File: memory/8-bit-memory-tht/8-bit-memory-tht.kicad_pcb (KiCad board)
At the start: 2 copper layers, 126 parts, among them J1 J1-1_bit_bus, J2 J8-8_bit_bus_connector, J3 J2-2_pole_connector, J4 J8-8_bit_bus_connector, Q1 2N7000, Q10 2N7000, Q11 2N7000, Q12 2N7000, Q13 2N7000, Q14 2N7000, Q15 2N7000, Q16 2N7000, Q17 2N7000, Q18 2N7000, Q19 2N7000, Q2 2N7000, Q20 2N7000, Q21 2N7000, Q22 2N7000, Q23 2N7000, Q24 2N7000, Q25 2N7000, Q26 2N7000, Q27 2N7000, Q28 2N7000, Q29 2N7000, Q3 2N7000, Q30 2N7000, Q31 2N7000, Q32 2N7000, Q33 2N7000, Q34 2N7000, Q35 2N7000, Q36 2N7000, Q37 2N7000, Q38 2N7000, Q39 2N7000, Q4 2N7000, Q40 2N7000, Q41 2N7000, Q42 2N7000, Q43 2N7000, Q44 2N7000, Q45 2N7000, Q46 2N7000, Q47 2N7000, Q48 2N7000, Q49 2N7000, Q5 2N7000, Q50 2N7000, Q51 2N7000, Q52 2N7000, Q53 2N7000, Q54 2N7000, Q55 2N7000, Q56 2N7000, Q57 2N7000, Q58 2N7000, Q59 2N7000, Q6 2N7000, Q60 2N7000, Q61 2N7000, Q62 2N7000, Q63 2N7000, Q64 2N7000, Q65 2N7000, Q66 2N7000, Q67 2N7000, Q68 2N7000, Q69 2N7000, Q7 2N7000, Q70 2N7000, Q71 2N7000, Q72 2N7000, Q73 2N7000, Q8 2N7000, Q9 2N7000

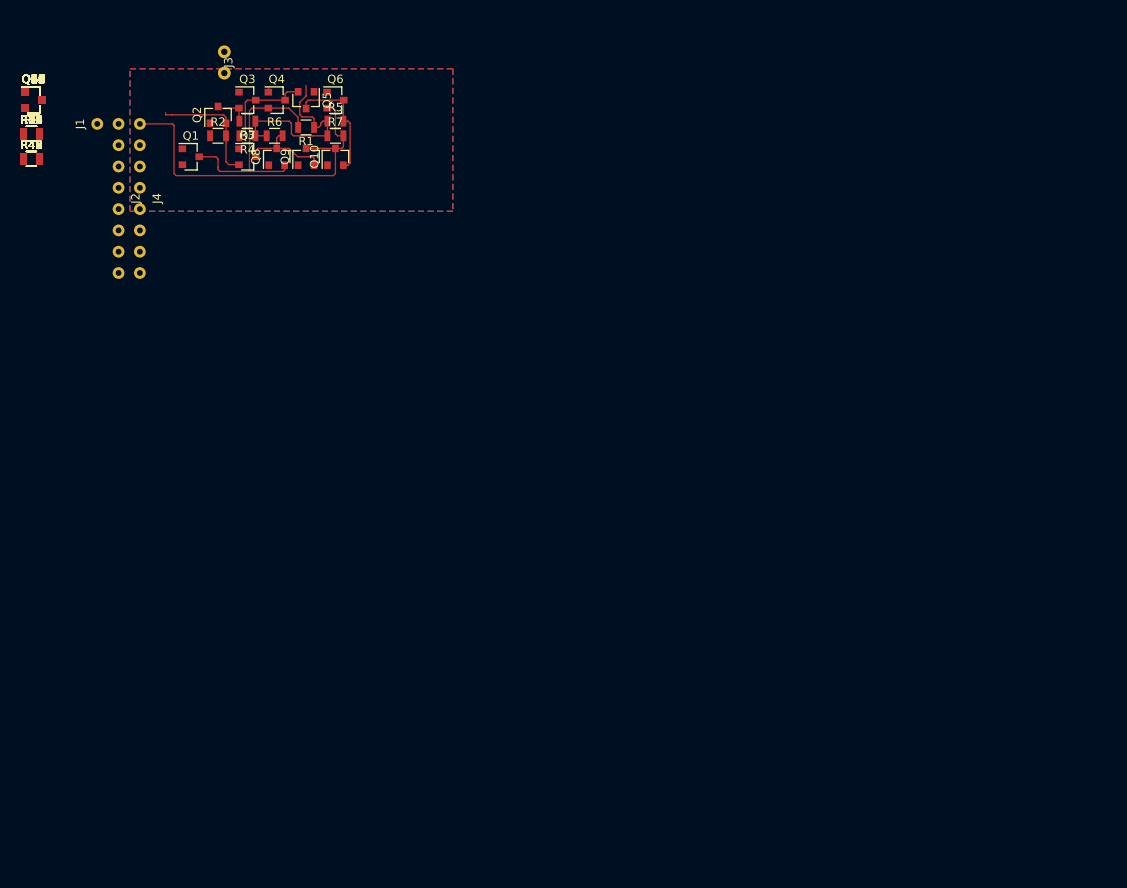
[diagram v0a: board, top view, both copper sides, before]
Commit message: Finish THT memory board layout
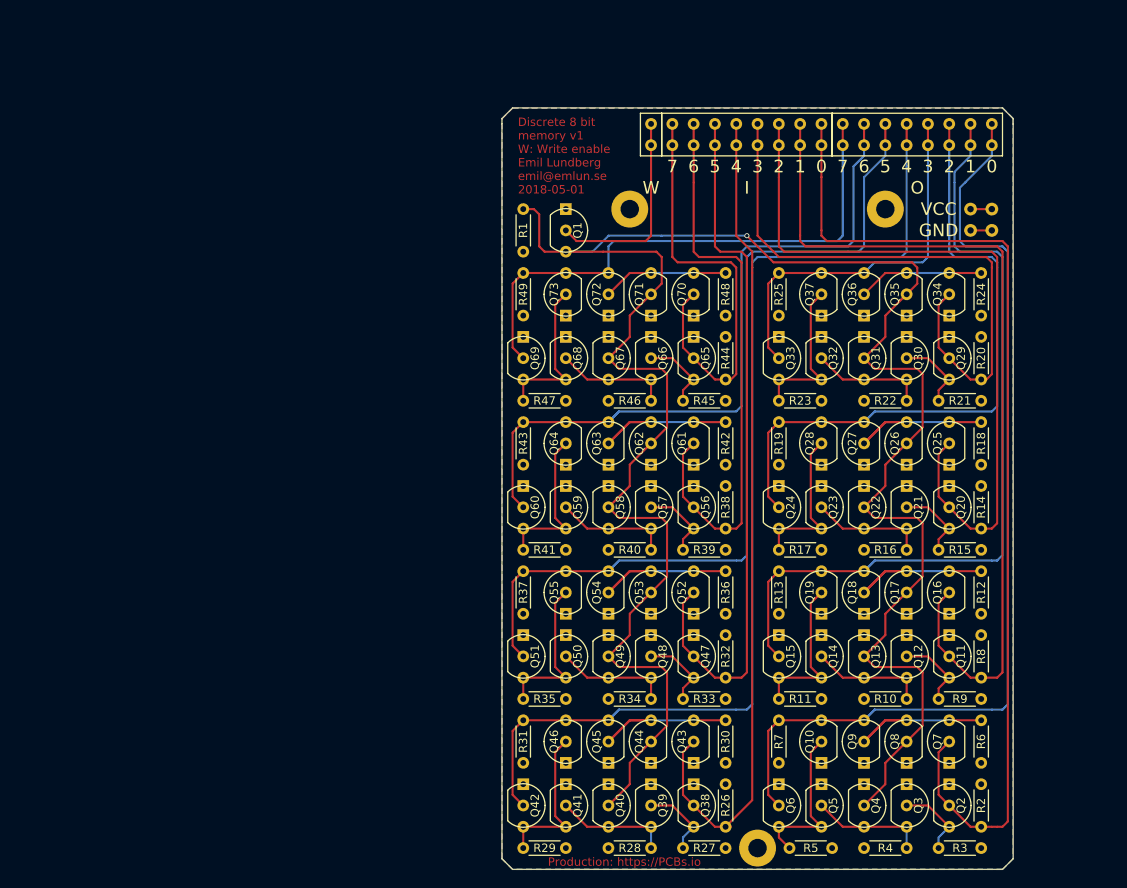
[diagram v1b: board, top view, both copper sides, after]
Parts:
- added REF**: MountingHole_2.2mm_M2_Pad, Mounting_Holes:MountingHole_2.2mm_M2_Pad, F.Cu at (165.1, 78.7)
- added REF**: MountingHole_2.2mm_M2_Pad, Mounting_Holes:MountingHole_2.2mm_M2_Pad, F.Cu at (195.6, 78.7)
- added REF**: MountingHole_2.2mm_M2_Pad, Mounting_Holes:MountingHole_2.2mm_M2_Pad, F.Cu at (180.3, 154.9)
- J1: footprint emlun:J1-1_bit_bus -> J1x2-double_1_bit_bus
- J2, J4: footprint emlun:J8-8_bit_bus_connector -> emlun:J8x2-double_8_bit_bus_connector
- J3: footprint emlun:J2-2_pole_connector -> J2x2-double_2_pole_connector
- Q1, Q10, Q11, Q12, Q13, Q14, Q15, Q16, Q17, Q18, Q19, Q2, Q20, Q21, Q22, Q23, Q24, Q25, Q26, Q27, Q28, Q29, Q3, Q30, Q31, Q32, Q33, Q35, Q36, Q37, Q38, Q39, Q4, Q40, Q41, Q42, Q43, Q44, Q45, Q46, Q47, Q48, Q49, Q5, Q50, Q51, Q52, Q53, Q54, Q55, Q56, Q57, Q58, Q59, Q6, Q60, Q61, Q62, Q63, Q64, Q65, Q66, Q67, Q68, Q69, Q7, Q70, Q71, Q72, Q73, Q8, Q9: footprint TO_SOT_Packages_SMD:SOT-23 -> electrokit:TO-92_Molded_Wide_Inline
- Q34: footprint TO_SOT_Packages_SMD:SOT-23 -> TO-92_Molded_Wide_Inline
- R1, R10, R11, R12, R13, R14, R15, R16, R17, R18, R19, R2, R20, R21, R22, R23, R24, R25, R26, R27, R28, R29, R3, R30, R31, R32, R33, R34, R35, R36, R37, R38, R39, R4, R40, R41, R42, R43, R44, R45, R46, R47, R48, R49, R5, R6, R7, R8, R9: footprint Resistors_SMD:R_0805 -> emlun:R_Axial_DIN0204_L3.6mm_D1.6mm_P5.08mm_Horizontal
- moved R9 131.8 mm to (207.0, 137.2), turned to 180 degrees
- moved R8 128.1 mm to (207.0, 129.5), turned to 270 degrees
- moved Q11 127.8 mm to (203.2, 132.1), turned to 270 degrees
- moved R12 126.9 mm to (207.0, 127.0), turned to 90 degrees
- moved Q16 124.0 mm to (203.2, 124.5), turned to 90 degrees
- moved R15 123.7 mm to (207.0, 119.4), turned to 180 degrees
- moved Q12 123.5 mm to (198.1, 132.1), turned to 270 degrees
- moved R3 123.2 mm to (207.0, 154.9)
- moved R14 120.8 mm to (207.0, 111.8), turned to 270 degrees
- moved R10 120.0 mm to (193.0, 137.2)
- moved Q2 119.9 mm to (203.2, 149.9), turned to 270 degrees
- moved R18 119.9 mm to (207.0, 109.2), turned to 90 degrees
- moved Q17 119.5 mm to (198.1, 124.5), turned to 90 degrees
- moved Q20 119.5 mm to (203.2, 114.3), turned to 270 degrees
- moved R2 119.4 mm to (207.0, 147.3), turned to 270 degrees
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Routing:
- net /notW: track 27.2 -> 252.8 mm, vias 0 -> 1
- net /O4: track 0.00 -> 128.0 mm
- net /I0: track 14.6 -> 122.3 mm
- net /O5: track 0.00 -> 106.2 mm
- net /I1: track 0.00 -> 105.8 mm
- net /I4: track 0.00 -> 100.1 mm
- net /O1: track 0.00 -> 97.7 mm
- net /I2: track 0.00 -> 89.3 mm
- net /O6: track 0.00 -> 86.6 mm
- net /I5: track 0.00 -> 85.4 mm
- net /O2: track 0.00 -> 78.5 mm
- net /O0: track 43.2 -> 116.9 mm
- net /I3: track 0.00 -> 71.0 mm
- net /I6: track 0.00 -> 68.9 mm
- net /O7: track 0.00 -> 66.3 mm
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- added copper zone on F.Cu, net VCC
- removed copper zone on F.Cu, net GND
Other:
- board outline added: 61 x 90.8 mm
- board text added: "0"
- board text added: "1"
- board text added: "2"
- board text added: "3"
- board text added: "4"
- board text added: "5"
- board text added: "6"
- board text added: "7"
- board text added: "Discrete 8 bit memory v1 W: Write enable Emil Lundberg emil@emlun.se 2018-05-01"
- board text added: "GND"
- board text added: "I"
- board text added: "O"
- board text added: "Production: https://PCBs.io"
- board text added: "VCC"
- board text added: "W"

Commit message: Add THT memory circuit v2
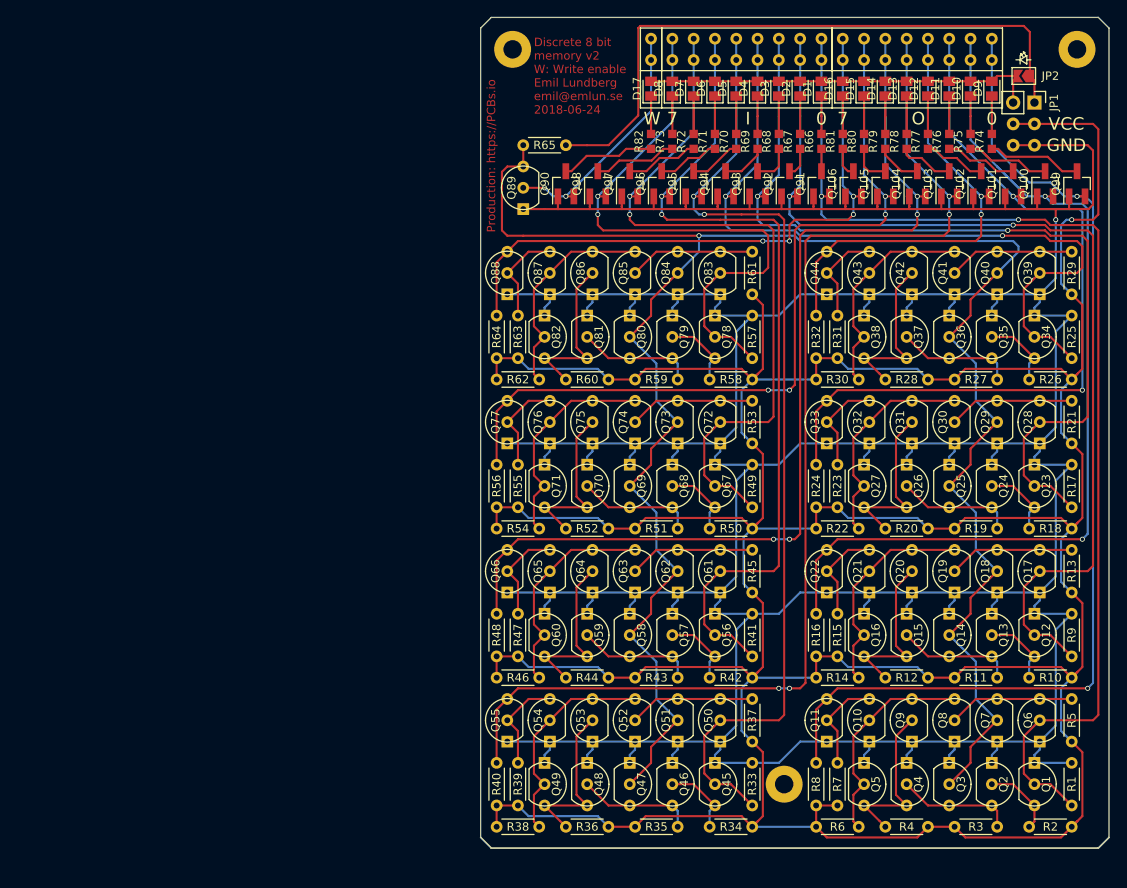
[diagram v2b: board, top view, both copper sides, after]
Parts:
- added D1: LED, LED_SMD:LED_0805_2012Metric_Pad1.12x1.40mm_HandSolder, F.Cu at (188.0, 64.4)
- added D10: LED, LED_SMD:LED_0805_2012Metric_Pad1.12x1.40mm_HandSolder, F.Cu at (205.7, 64.4)
- added D11: LED, LED_SMD:LED_0805_2012Metric_Pad1.12x1.40mm_HandSolder, F.Cu at (203.2, 64.4)
- added D12: LED, LED_SMD:LED_0805_2012Metric_Pad1.12x1.40mm_HandSolder, F.Cu at (200.7, 64.4)
- added D13: LED, LED_SMD:LED_0805_2012Metric_Pad1.12x1.40mm_HandSolder, F.Cu at (198.1, 64.4)
- added D14: LED, LED_SMD:LED_0805_2012Metric_Pad1.12x1.40mm_HandSolder, F.Cu at (195.6, 64.4)
- added D15: LED, LED_SMD:LED_0805_2012Metric_Pad1.12x1.40mm_HandSolder, F.Cu at (193.0, 64.4)
- added D16: LED, LED_SMD:LED_0805_2012Metric_Pad1.12x1.40mm_HandSolder, F.Cu at (190.5, 64.4)
- added D17: LED, LED_SMD:LED_0805_2012Metric_Pad1.12x1.40mm_HandSolder, F.Cu at (167.6, 64.4)
- added D2: LED, LED_SMD:LED_0805_2012Metric_Pad1.12x1.40mm_HandSolder, F.Cu at (185.4, 64.4)
- added D3: LED, LED_SMD:LED_0805_2012Metric_Pad1.12x1.40mm_HandSolder, F.Cu at (182.9, 64.4)
- added D4: LED, LED_SMD:LED_0805_2012Metric_Pad1.12x1.40mm_HandSolder, F.Cu at (180.3, 64.4)
- added D5: LED, LED_SMD:LED_0805_2012Metric_Pad1.12x1.40mm_HandSolder, F.Cu at (177.8, 64.4)
- added D6: LED, LED_SMD:LED_0805_2012Metric_Pad1.12x1.40mm_HandSolder, F.Cu at (175.3, 64.4)
- added D7: LED, LED_SMD:LED_0805_2012Metric_Pad1.12x1.40mm_HandSolder, F.Cu at (172.7, 64.4)
- added D8: LED, LED_SMD:LED_0805_2012Metric_Pad1.12x1.40mm_HandSolder, F.Cu at (170.2, 64.4)
- added D9: LED, LED_SMD:LED_0805_2012Metric_Pad1.12x1.40mm_HandSolder, F.Cu at (208.3, 64.4)
- added JP1: Jumper_2_Open, Connector_PinHeader_2.54mm:PinHeader_1x02_P2.54mm_Vertical, F.Cu at (213.4, 66.0)
- added JP2: SolderJumper_2_Bridged, Jumper:SolderJumper-2_P1.3mm_Open_TrianglePad1.0x1.5mm, F.Cu at (212.1, 62.9)
- added Q100: 2N7000, Package_TO_SOT_SMD:SOT-23_Handsoldering, F.Cu at (214.6, 75.7)
- added Q101: 2N7000, Package_TO_SOT_SMD:SOT-23_Handsoldering, F.Cu at (210.8, 75.7)
- added Q102: 2N7000, Package_TO_SOT_SMD:SOT-23_Handsoldering, F.Cu at (207.0, 75.7)
- added Q103: 2N7000, Package_TO_SOT_SMD:SOT-23_Handsoldering, F.Cu at (203.2, 75.7)
- added Q104: 2N7000, Package_TO_SOT_SMD:SOT-23_Handsoldering, F.Cu at (199.4, 75.7)
- added Q105: 2N7000, Package_TO_SOT_SMD:SOT-23_Handsoldering, F.Cu at (195.6, 75.7)
- added Q106: 2N7000, Package_TO_SOT_SMD:SOT-23_Handsoldering, F.Cu at (191.8, 75.7)
- added Q74: 2N7000, electrokit:TO-92_Molded_Wide_Inline, F.Cu at (165.7, 104.1)
- added Q75: 2N7000, electrokit:TO-92_Molded_Wide_Inline, F.Cu at (160.7, 104.1)
- added Q76: 2N7000, electrokit:TO-92_Molded_Wide_Inline, F.Cu at (155.6, 104.1)
- added Q77: 2N7000, electrokit:TO-92_Molded_Wide_Inline, F.Cu at (150.5, 104.1)
- added Q78: 2N7000, electrokit:TO-92_Molded_Wide_Inline, F.Cu at (175.3, 94.0)
- added Q79: 2N7000, electrokit:TO-92_Molded_Wide_Inline, F.Cu at (170.2, 94.0)
- added Q80: 2N7000, electrokit:TO-92_Molded_Wide_Inline, F.Cu at (165.1, 94.0)
- added Q81: 2N7000, electrokit:TO-92_Molded_Wide_Inline, F.Cu at (160.0, 94.0)
- added Q82: 2N7000, electrokit:TO-92_Molded_Wide_Inline, F.Cu at (154.9, 94.0)
- added Q83: 2N7000, electrokit:TO-92_Molded_Wide_Inline, F.Cu at (175.9, 86.4)
- added Q84: 2N7000, electrokit:TO-92_Molded_Wide_Inline, F.Cu at (170.8, 86.4)
- added Q85: 2N7000, electrokit:TO-92_Molded_Wide_Inline, F.Cu at (165.7, 86.4)
- added Q86: 2N7000, electrokit:TO-92_Molded_Wide_Inline, F.Cu at (160.7, 86.4)
- added Q87: 2N7000, electrokit:TO-92_Molded_Wide_Inline, F.Cu at (155.6, 86.4)
- added Q88: 2N7000, electrokit:TO-92_Molded_Wide_Inline, F.Cu at (150.5, 86.4)
- added Q89: 2N7000, electrokit:TO-92_Molded_Wide_Inline, F.Cu at (152.4, 76.2)
- added Q90: 2N7000, Package_TO_SOT_SMD:SOT-23_Handsoldering, F.Cu at (157.5, 75.7)
- added Q91: 2N7000, Package_TO_SOT_SMD:SOT-23_Handsoldering, F.Cu at (188.0, 75.7)
- added Q92: 2N7000, Package_TO_SOT_SMD:SOT-23_Handsoldering, F.Cu at (184.2, 75.7)
- added Q93: 2N7000, Package_TO_SOT_SMD:SOT-23_Handsoldering, F.Cu at (180.3, 75.7)
- added Q94: 2N7000, Package_TO_SOT_SMD:SOT-23_Handsoldering, F.Cu at (176.5, 75.7)
- added Q95: 2N7000, Package_TO_SOT_SMD:SOT-23_Handsoldering, F.Cu at (172.7, 75.7)
- added Q96: 2N7000, Package_TO_SOT_SMD:SOT-23_Handsoldering, F.Cu at (168.9, 75.7)
- added Q97: 2N7000, Package_TO_SOT_SMD:SOT-23_Handsoldering, F.Cu at (165.1, 75.7)
- added Q98: 2N7000, Package_TO_SOT_SMD:SOT-23_Handsoldering, F.Cu at (161.3, 75.7)
- added Q99: 2N7000, Package_TO_SOT_SMD:SOT-23_Handsoldering, F.Cu at (218.4, 75.7)
- added R50: R, Resistor_THT:R_Axial_DIN0204_L3.6mm_D1.6mm_P5.08mm_Horizontal, F.Cu at (179.7, 116.8)
- added R51: R, Resistor_THT:R_Axial_DIN0204_L3.6mm_D1.6mm_P5.08mm_Horizontal, F.Cu at (165.7, 116.8)
- added R52: R, Resistor_THT:R_Axial_DIN0204_L3.6mm_D1.6mm_P5.08mm_Horizontal, F.Cu at (162.6, 116.8)
- added R53: R, Resistor_THT:R_Axial_DIN0204_L3.6mm_D1.6mm_P5.08mm_Horizontal, F.Cu at (179.7, 106.7)
- added R54: R, Resistor_THT:R_Axial_DIN0204_L3.6mm_D1.6mm_P5.08mm_Horizontal, F.Cu at (149.2, 116.8)
- added R55: R, Resistor_THT:R_Axial_DIN0204_L3.6mm_D1.6mm_P5.08mm_Horizontal, F.Cu at (151.8, 114.3)
- added R56: R, Resistor_THT:R_Axial_DIN0204_L3.6mm_D1.6mm_P5.08mm_Horizontal, F.Cu at (149.2, 114.3)
- added R57: R, Resistor_THT:R_Axial_DIN0204_L3.6mm_D1.6mm_P5.08mm_Horizontal, F.Cu at (179.7, 91.4)
- added R58: R, Resistor_THT:R_Axial_DIN0204_L3.6mm_D1.6mm_P5.08mm_Horizontal, F.Cu at (179.7, 99.1)
- added R59: R, Resistor_THT:R_Axial_DIN0204_L3.6mm_D1.6mm_P5.08mm_Horizontal, F.Cu at (165.7, 99.1)
- added R60: R, Resistor_THT:R_Axial_DIN0204_L3.6mm_D1.6mm_P5.08mm_Horizontal, F.Cu at (162.6, 99.1)
- added R61: R, Resistor_THT:R_Axial_DIN0204_L3.6mm_D1.6mm_P5.08mm_Horizontal, F.Cu at (179.7, 88.9)
- added R62: R, Resistor_THT:R_Axial_DIN0204_L3.6mm_D1.6mm_P5.08mm_Horizontal, F.Cu at (149.2, 99.1)
- added R63: R, Resistor_THT:R_Axial_DIN0204_L3.6mm_D1.6mm_P5.08mm_Horizontal, F.Cu at (151.8, 96.5)
- added R64: R, Resistor_THT:R_Axial_DIN0204_L3.6mm_D1.6mm_P5.08mm_Horizontal, F.Cu at (149.2, 96.5)
- added R65: R, Resistor_THT:R_Axial_DIN0204_L3.6mm_D1.6mm_P5.08mm_Horizontal, F.Cu at (157.5, 71.1)
- added R66: R, Resistor_SMD:R_0603_1608Metric_Pad0.99x1.00mm_HandSolder, F.Cu at (188.0, 70.7)
- added R67: R, Resistor_SMD:R_0603_1608Metric_Pad0.99x1.00mm_HandSolder, F.Cu at (185.4, 70.7)
- added R68: R, Resistor_SMD:R_0603_1608Metric_Pad0.99x1.00mm_HandSolder, F.Cu at (182.9, 70.7)
- added R69: R, Resistor_SMD:R_0603_1608Metric_Pad0.99x1.00mm_HandSolder, F.Cu at (180.3, 70.7)
- added R70: R, Resistor_SMD:R_0603_1608Metric_Pad0.99x1.00mm_HandSolder, F.Cu at (177.8, 70.7)
- added R71: R, Resistor_SMD:R_0603_1608Metric_Pad0.99x1.00mm_HandSolder, F.Cu at (175.3, 70.7)
- added R72: R, Resistor_SMD:R_0603_1608Metric_Pad0.99x1.00mm_HandSolder, F.Cu at (172.7, 70.7)
- added R73: R, Resistor_SMD:R_0603_1608Metric_Pad0.99x1.00mm_HandSolder, F.Cu at (170.2, 70.7)
- added R74: R, Resistor_SMD:R_0603_1608Metric_Pad0.99x1.00mm_HandSolder, F.Cu at (208.3, 70.7)
- added R75: R, Resistor_SMD:R_0603_1608Metric_Pad0.99x1.00mm_HandSolder, F.Cu at (205.7, 70.7)
- added R76: R, Resistor_SMD:R_0603_1608Metric_Pad0.99x1.00mm_HandSolder, F.Cu at (203.2, 70.7)
- added R77: R, Resistor_SMD:R_0603_1608Metric_Pad0.99x1.00mm_HandSolder, F.Cu at (200.7, 70.7)
- added R78: R, Resistor_SMD:R_0603_1608Metric_Pad0.99x1.00mm_HandSolder, F.Cu at (198.1, 70.7)
- added R79: R, Resistor_SMD:R_0603_1608Metric_Pad0.99x1.00mm_HandSolder, F.Cu at (195.6, 70.7)
- added R80: R, Resistor_SMD:R_0603_1608Metric_Pad0.99x1.00mm_HandSolder, F.Cu at (193.0, 70.7)
- added R81: R, Resistor_SMD:R_0603_1608Metric_Pad0.99x1.00mm_HandSolder, F.Cu at (190.5, 70.7)
- added R82: R, Resistor_SMD:R_0603_1608Metric_Pad0.99x1.00mm_HandSolder, F.Cu at (167.6, 70.7)
- J1: footprint J1x2-double_1_bit_bus -> emlun:J1x2-double_1_bit_bus
- J3: value J2-2_pole_connector -> J8-8_bit_bus_connector; footprint J2x2-double_2_pole_connector -> emlun:J8x2-double_8_bit_bus_connector
- J4: value J8-8_bit_bus_connector -> PWR-2_pole_power_connector; footprint emlun:J8x2-double_8_bit_bus_connector -> emlun:J2x2-double_2_pole_connector
- Q34: footprint TO-92_Molded_Wide_Inline -> electrokit:TO-92_Molded_Wide_Inline
- R1, R10, R11, R12, R13, R14, R15, R16, R17, R18, R19, R2, R20, R21, R22, R23, R24, R25, R26, R27, R28, R29, R3, R30, R31, R32, R33, R34, R35, R36, R37, R38, R39, R4, R40, R41, R42, R43, R44, R45, R46, R47, R48, R49, R5, R6, R7, R8, R9: footprint emlun:R_Axial_DIN0204_L3.6mm_D1.6mm_P5.08mm_Horizontal -> Resistor_THT:R_Axial_DIN0204_L3.6mm_D1.6mm_P5.08mm_Horizontal
- moved R29 89.4 mm to (217.8, 88.9), turned to 90 degrees
- moved R1 89.4 mm to (217.8, 144.8), turned to 270 degrees
- moved Q1 86.5 mm to (213.4, 147.3)
- moved Q39 78.6 mm to (214.0, 86.4), turned to 90 degrees
- moved Q41 78.6 mm to (203.8, 86.4), turned to 90 degrees
- moved Q40 78.6 mm to (208.9, 86.4), turned to 90 degrees
- moved Q42 78.6 mm to (198.8, 86.4), turned to 90 degrees
- moved R28 67.6 mm to (200.7, 99.1), turned to 180 degrees
- moved R26 63.5 mm to (217.8, 99.1), turned to 180 degrees
- moved R27 62.2 mm to (203.8, 99.1), turned to 0 degrees
- moved R31 61.1 mm to (189.9, 96.5)
- moved Q43 59.7 mm to (193.7, 86.4)
- moved Q44 59.7 mm to (188.6, 86.4)
- moved Q38 59.5 mm to (193.0, 94.0)
- moved REF** 56.6 mm to (218.4, 59.7)
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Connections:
- J3 pad 1: GND -> /O1
- J3 pad 2: VCC -> /O2
- J4 pad 1: /O1 -> GND
- J4 pad 2: /O2 -> VCC
- Q1 pad 2: /W -> /I0
- Q1 pad 3: /notW -> Net-(Q1-Pad3)
- Q10 pad 2: Net-(Q10-Pad2) -> /FB0
- Q10 pad 3: /O0 -> Net-(Q10-Pad3)
- Q11 pad 2: /I1 -> Net-(Q10-Pad3)
- Q11 pad 3: Net-(Q11-Pad3) -> /O0
- Q12 pad 2: Net-(Q11-Pad3) -> /I1
- Q13 pad 2: /notW -> Net-(Q12-Pad3)
- Q13 pad 3: Net-(Q12-Pad3) -> Net-(Q13-Pad3)
- Q14 pad 2: Net-(Q12-Pad3) -> /notW
- Q14 pad 3: Net-(Q14-Pad3) -> Net-(Q13-Pad3)
- Q15 pad 2: /O1 -> Net-(Q13-Pad3)
- Q15 pad 3: Net-(Q14-Pad3) -> Net-(Q15-Pad3)
- Q16 pad 2: /I1 -> /FB1
- Q16 pad 3: Net-(Q16-Pad3) -> Net-(Q15-Pad3)
- Q17 pad 2: /notW -> /I1
- Q17 pad 3: Net-(Q16-Pad3) -> Net-(Q17-Pad3)
- Q18 pad 2: Net-(Q16-Pad3) -> /notW
- Q18 pad 3: /O1 -> Net-(Q17-Pad3)
- Q19 pad 2: Net-(Q14-Pad3) -> Net-(Q17-Pad3)
- Q19 pad 3: /O1 -> /FB1
- Q2 pad 2: /I0 -> Net-(Q1-Pad3)
- Q20 pad 2: /I2 -> Net-(Q15-Pad3)
- Q20 pad 3: Net-(Q20-Pad3) -> /FB1
- Q21 pad 2: Net-(Q20-Pad3) -> /FB1
- Q22 pad 2: /notW -> Net-(Q21-Pad3)
- Q22 pad 3: Net-(Q21-Pad3) -> /O1
- Q23 pad 2: Net-(Q21-Pad3) -> /I2
- Q24 pad 2: /O2 -> Net-(Q23-Pad3)
- Q24 pad 3: Net-(Q23-Pad3) -> Net-(Q24-Pad3)
- Q25 pad 2: /I2 -> /notW
- Q25 pad 3: Net-(Q25-Pad3) -> Net-(Q24-Pad3)
- Q26 pad 2: /notW -> Net-(Q24-Pad3)
- Q26 pad 3: Net-(Q25-Pad3) -> Net-(Q26-Pad3)
- Q27 pad 2: Net-(Q25-Pad3) -> /FB2
- Q27 pad 3: /O2 -> Net-(Q26-Pad3)
- Q28 pad 2: Net-(Q23-Pad3) -> /I2
- Q28 pad 3: /O2 -> Net-(Q28-Pad3)
- Q29 pad 2: /I3 -> /notW
- Q29 pad 3: Net-(Q29-Pad3) -> Net-(Q28-Pad3)
- Q3 pad 2: Net-(Q2-Pad3) -> /notW
- Q3 pad 3: Net-(Q3-Pad3) -> Net-(Q2-Pad3)
- Q30 pad 2: Net-(Q29-Pad3) -> Net-(Q28-Pad3)
- Q30 pad 3: Net-(Q30-Pad3) -> /FB2
- Q31 pad 2: /notW -> Net-(Q26-Pad3)
- Q31 pad 3: Net-(Q30-Pad3) -> /FB2
- Q32 pad 2: Net-(Q30-Pad3) -> /FB2
- Q33 pad 2: /O3 -> Net-(Q32-Pad3)
- Q33 pad 3: Net-(Q32-Pad3) -> /O2
- Q35 pad 2: /notW -> Net-(Q34-Pad3)
- Q35 pad 3: Net-(Q34-Pad3) -> Net-(Q35-Pad3)
- Q36 pad 2: Net-(Q34-Pad3) -> /notW
- Q36 pad 3: /O3 -> Net-(Q35-Pad3)
- Q37 pad 2: Net-(Q32-Pad3) -> Net-(Q35-Pad3)
- Q37 pad 3: /O3 -> Net-(Q37-Pad3)
- Q38 pad 2: /I4 -> /FB3
- Q38 pad 3: Net-(Q38-Pad3) -> Net-(Q37-Pad3)
- Q39 pad 2: Net-(Q38-Pad3) -> /I3
- Q4 pad 2: /notW -> Net-(Q2-Pad3)
- Q4 pad 3: Net-(Q3-Pad3) -> Net-(Q4-Pad3)
- Q41 pad 3: Net-(Q41-Pad3) -> /FB3
- Q42 pad 2: /O4 -> Net-(Q37-Pad3)
- Q42 pad 3: Net-(Q41-Pad3) -> /FB3
- Q43 pad 2: /I4 -> /FB3
- Q44 pad 2: /notW -> Net-(Q43-Pad3)
- Q44 pad 3: Net-(Q43-Pad3) -> /O3
- Q45 pad 2: Net-(Q43-Pad3) -> /I4
- Q45 pad 3: /O4 -> Net-(Q45-Pad3)
- Q46 pad 2: Net-(Q41-Pad3) -> Net-(Q45-Pad3)
- Q46 pad 3: /O4 -> Net-(Q46-Pad3)
- Q47 pad 2: /I5 -> /notW
- Q47 pad 3: Net-(Q47-Pad3) -> Net-(Q46-Pad3)
- Q48 pad 2: Net-(Q47-Pad3) -> Net-(Q46-Pad3)
- Q49 pad 2: /notW -> /FB4
- Q5 pad 2: Net-(Q3-Pad3) -> /FB0
- Q5 pad 3: Net-(Q10-Pad2) -> Net-(Q4-Pad3)
- Q50 pad 2: Net-(Q48-Pad3) -> /I4
- Q51 pad 2: /O5 -> /notW
- Q52 pad 2: /I5 -> Net-(Q50-Pad3)
- Q52 pad 3: Net-(Q52-Pad3) -> /FB4
- Q53 pad 2: /notW -> Net-(Q48-Pad3)
- Q53 pad 3: Net-(Q52-Pad3) -> /FB4
- Q54 pad 2: Net-(Q52-Pad3) -> /FB4
- Q54 pad 3: /O5 -> Net-(Q54-Pad3)
- Q55 pad 2: Net-(Q50-Pad3) -> Net-(Q54-Pad3)
- Q55 pad 3: /O5 -> /O4
- Q56 pad 2: /I6 -> /I5
- Q6 pad 2: /O0 -> /I0
- Q6 pad 3: Net-(Q10-Pad2) -> Net-(Q6-Pad3)
- Q60 pad 2: /O6 -> /FB5
- Q61 pad 2: /I6 -> /I5
- Q63 pad 3: /O6 -> /FB5
- Q64 pad 3: /O6 -> /FB5
- Q65 pad 2: /I7 -> /FB5
- Q66 pad 3: Net-(Q66-Pad3) -> /O5
- Q67 pad 2: /notW -> /I6
- Q67 pad 3: Net-(Q66-Pad3) -> Net-(Q67-Pad3)
- Q68 pad 2: Net-(Q66-Pad3) -> Net-(Q67-Pad3)
- Q69 pad 2: /O7 -> /notW
- Q7 pad 2: /I0 -> /notW
- Q7 pad 3: Net-(Q7-Pad3) -> Net-(Q6-Pad3)
- Q70 pad 2: /I7 -> Net-(Q68-Pad3)
- Q71 pad 2: /notW -> /FB6
- Q72 pad 2: Net-(Q70-Pad3) -> /I6
- Q72 pad 3: /O7 -> Net-(Q72-Pad3)
- Q73 pad 2: Net-(Q68-Pad3) -> /notW
- Q73 pad 3: /O7 -> Net-(Q72-Pad3)
- Q8 pad 2: /notW -> Net-(Q6-Pad3)
- Q8 pad 3: Net-(Q7-Pad3) -> /FB0
- Q9 pad 2: Net-(Q7-Pad3) -> Net-(Q4-Pad3)
- Q9 pad 3: /O0 -> /FB0
- R1 pad 1: VCC -> GND
- R1 pad 2: /notW -> /I0
- R11 pad 2: Net-(Q14-Pad3) -> Net-(Q13-Pad3)
- R12 pad 2: Net-(Q16-Pad3) -> Net-(Q15-Pad3)
- R13 pad 2: /O1 -> Net-(Q17-Pad3)
- R14 pad 1: GND -> VCC
- R14 pad 2: /I2 -> /FB1
- R15 pad 2: Net-(Q20-Pad3) -> Net-(Q21-Pad3)
- R16 pad 2: Net-(Q21-Pad3) -> /O1
- R17 pad 1: VCC -> GND
- R17 pad 2: Net-(Q23-Pad3) -> /I2
- R18 pad 2: Net-(Q25-Pad3) -> Net-(Q23-Pad3)
- R19 pad 2: /O2 -> Net-(Q24-Pad3)
- R2 pad 1: GND -> VCC
- R2 pad 2: /I0 -> Net-(Q1-Pad3)
- R20 pad 1: GND -> VCC
- R20 pad 2: /I3 -> Net-(Q26-Pad3)
- R21 pad 2: Net-(Q29-Pad3) -> Net-(Q28-Pad3)
- R22 pad 2: Net-(Q30-Pad3) -> /FB2
- R24 pad 2: Net-(Q34-Pad3) -> /O2
- R25 pad 1: VCC -> GND
- R25 pad 2: /O3 -> /I3
- R26 pad 1: GND -> VCC
- R26 pad 2: /I4 -> Net-(Q34-Pad3)
- R27 pad 2: Net-(Q38-Pad3) -> Net-(Q35-Pad3)
- R28 pad 2: Net-(Q39-Pad3) -> Net-(Q37-Pad3)
- R29 pad 2: Net-(Q41-Pad3) -> Net-(Q39-Pad3)
- R30 pad 2: Net-(Q43-Pad3) -> /FB3
- R31 pad 2: /O4 -> Net-(Q43-Pad3)
- R32 pad 1: GND -> VCC
- R32 pad 2: /I5 -> /O3
- R33 pad 1: VCC -> GND
- R33 pad 2: Net-(Q47-Pad3) -> /I4
- R34 pad 2: Net-(Q48-Pad3) -> Net-(Q45-Pad3)
- R35 pad 2: Net-(Q50-Pad3) -> Net-(Q46-Pad3)
- R36 pad 2: Net-(Q52-Pad3) -> Net-(Q48-Pad3)
- R37 pad 2: /O5 -> Net-(Q50-Pad3)
- R38 pad 1: GND -> VCC
- R38 pad 2: /I6 -> /FB4
- R39 pad 2: Net-(Q56-Pad3) -> Net-(Q54-Pad3)
- R4 pad 2: Net-(Q3-Pad3) -> Net-(Q4-Pad3)
- R40 pad 2: Net-(Q57-Pad3) -> /O4
- R41 pad 1: VCC -> GND
- R41 pad 2: Net-(Q59-Pad3) -> /I5
- R42 pad 2: Net-(Q61-Pad3) -> Net-(Q56-Pad3)
- R43 pad 2: /O6 -> Net-(Q57-Pad3)
- R44 pad 1: GND -> VCC
- R44 pad 2: /I7 -> Net-(Q59-Pad3)
- R45 pad 2: Net-(Q65-Pad3) -> Net-(Q61-Pad3)
- R46 pad 2: Net-(Q66-Pad3) -> /FB5
- R47 pad 2: Net-(Q68-Pad3) -> Net-(Q65-Pad3)
- R48 pad 2: Net-(Q70-Pad3) -> /O5
- R49 pad 1: VCC -> GND
- R49 pad 2: /O7 -> /I6
- R5 pad 2: Net-(Q10-Pad2) -> Net-(Q6-Pad3)
- R6 pad 2: Net-(Q7-Pad3) -> /FB0
- R7 pad 2: /O0 -> Net-(Q10-Pad3)
- R8 pad 1: GND -> VCC
- R8 pad 2: /I1 -> /O0
- R9 pad 1: VCC -> GND
- R9 pad 2: Net-(Q11-Pad3) -> /I1
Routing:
- net GND: track 2.54 -> 612.7 mm, vias 0 -> 1
- net VCC: track 2.54 -> 574.1 mm, vias 0 -> 1
- net Net-(D1-Pad2): track 0.00 -> 47.4 mm
- net /FB5: track 0.00 -> 26.0 mm
- net /FB4: track 0.00 -> 26.0 mm
- net /FB7: track 0.00 -> 26.0 mm
- net /FB6: track 0.00 -> 26.0 mm
- net /FB1: track 0.00 -> 26.0 mm
- net /FB2: track 0.00 -> 26.0 mm
- net /FB0: track 0.00 -> 26.0 mm
- net /FB3: track 0.00 -> 26.0 mm
- net Net-(Q7-Pad3): track 21.2 -> 0.00 mm
- net Net-(Q25-Pad3): track 21.2 -> 0.00 mm
- net Net-(Q16-Pad3): track 21.2 -> 0.00 mm
- net Net-(Q52-Pad3): track 21.2 -> 0.00 mm
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- removed copper zone on B.Cu, net GND
- removed copper zone on F.Cu, net VCC
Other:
- board size 61 x 90.8 mm -> 74.9 x 99.1 mm
- board text added: "Discrete 8 bit memory v2 W: Write enable Emil Lundberg emil@emlun.se 2018-06-24"
- board text removed: "1"
- board text removed: "2"
- board text removed: "3"
- board text removed: "4"
- board text removed: "5"
- board text removed: "6"
- board text removed: "Discrete 8 bit memory v1 W: Write enable Emil Lundberg emil@emlun.se 2018-05-01"
